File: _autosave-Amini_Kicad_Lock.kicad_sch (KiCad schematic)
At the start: 42 parts, among them J1 Conn_01x02_Pin, J2 Conn_01x04, J3 Conn_01x04_Pin, U1 nRF5340-QKxx, X1 ${ALTIUM_VALUE}, X2 ${ALTIUM_VALUE}

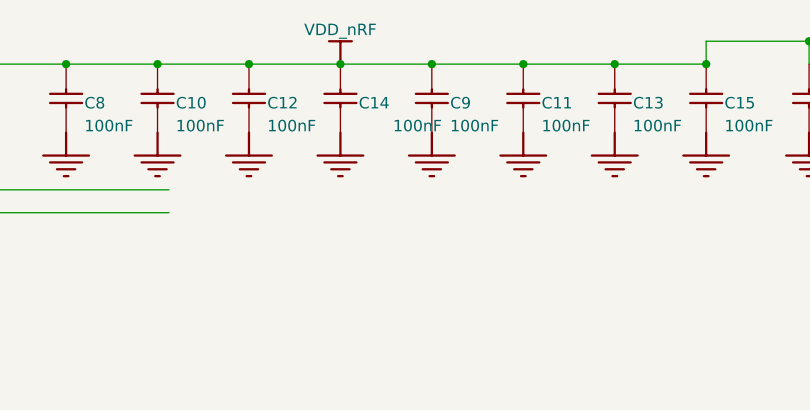
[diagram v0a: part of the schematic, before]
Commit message: fikset småting og endret logo
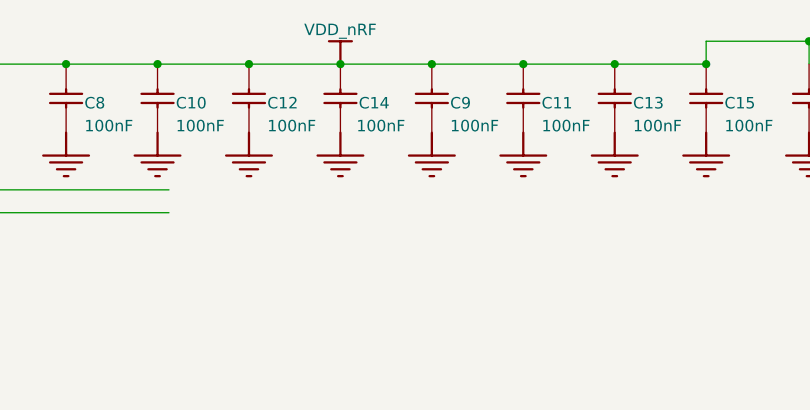
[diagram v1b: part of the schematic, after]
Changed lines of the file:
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@@
 		)
 		(property "Value" "${ALTIUM_VALUE}"
-			(at 219.202 22.86 0)
+			(at 215.138 22.86 0)
 			(effects
 				(font
